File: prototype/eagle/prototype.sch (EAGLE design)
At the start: 45 parts, among them J4 USBSMD, T1 3904, U1 ATMEGA328, U2 ATA6631, U3 ATA6631, U5 FT232RL, X1 16MHz

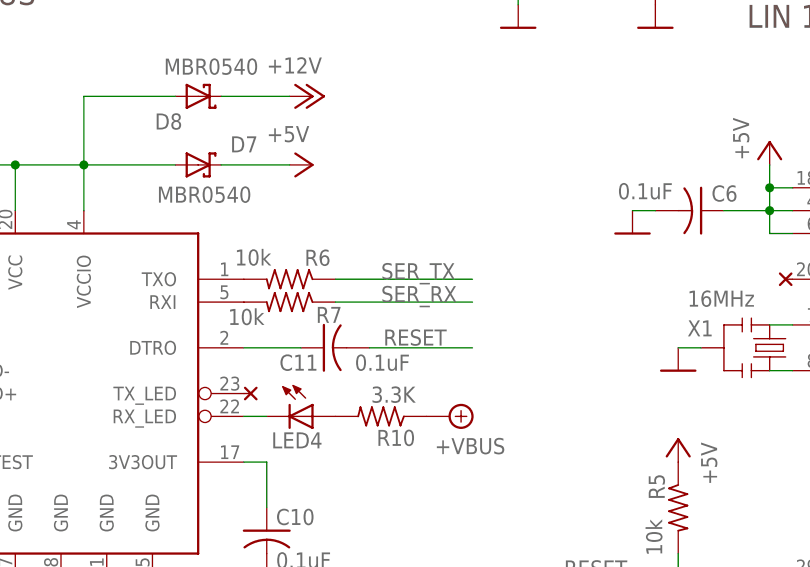
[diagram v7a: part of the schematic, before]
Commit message: Cleaned up the proxying code.
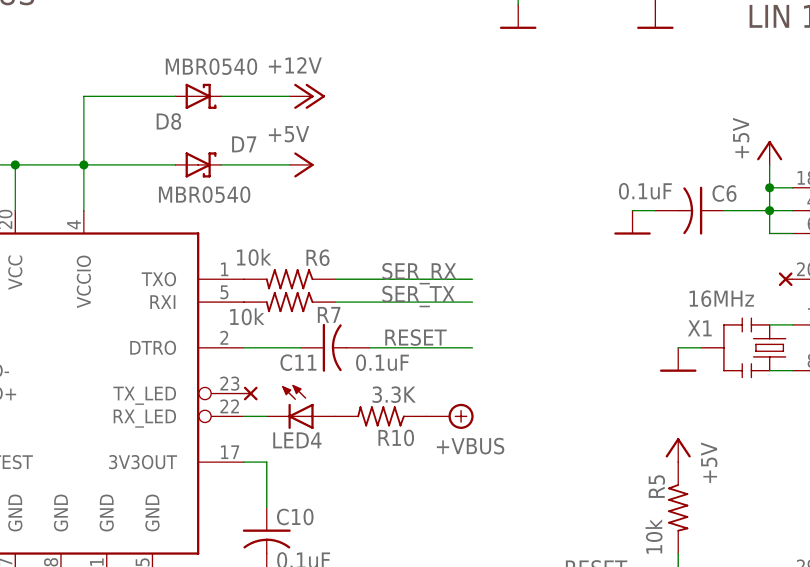
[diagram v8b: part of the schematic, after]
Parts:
- U1: device prototype:ATMEGA328 -> beeper:ATMEGA328
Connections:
- net SER_RX: now also R6.1; no longer R7.1
- net SER_TX: now also R7.1; no longer R6.1
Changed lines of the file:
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@@
 <layer number="51" name="tDocu" color="6" fill="1" visible="no" active="no"/>
 <layer number="52" name="bDocu" color="7" fill="1" visible="no" active="no"/>
-<layer number="53" name="tGND_GNDA" color="7" fill="9" visible="no" active="no"/>
-<layer number="54" name="bGND_GNDA" color="1" fill="9" visible="no" active="no"/>
+<layer number="53" name="tGND_GNDA" color="7" fill="1" visible="no" active="no"/>
+<layer number="54" name="bGND_GNDA" color="7" fill="1" visible="no" active="no"/>
 <layer number="56" name="wert" color="7" fill="1" visible="no" active="no"/>
 <layer number="91" name="Nets" color="2" fill="1" visible="yes" active="yes"/>
@@
 <layer number="97" name="Info" color="12" fill="1" visible="yes" active="yes"/>
 <layer number="98" name="Guide" color="6" fill="1" visible="yes" active="yes"/>
-<layer number="100" name="Muster" color="7" fill="1" visible="no" active="no"/>
-<layer number="101" name="Patch_Top" color="12" fill="4" visible="yes" active="yes"/>
+<layer number="100" name="Muster" color="7" fill="1" visible="yes" active="yes"/>
+<layer number="101" name="Patch_Top" color="7" fill="1" visible="yes" active="yes"/>
 <layer number="102" name="Vscore" color="7" fill="1" visible="yes" active="yes"/>
 <layer number="103" name="tMap" color="7" fill="1" visible="yes" active="yes"/>
@@
 <layer number="106" name="bPlate" color="7" fill="1" visible="yes" active="yes"/>
 <layer number="107" name="Crop" color="7" fill="1" visible="yes" active="yes"/>
-<layer number="116" name="Patch_BOT" color="9" fill="4" visible="yes" active="yes"/>
+<layer number="116" name="Patch_BOT" color="7" fill="1" visible="yes" active="yes"/>
 <layer number="121" name="_tsilk" color="7" fill="1" visible="yes" active="yes"/>
 <layer number="122" name="_bsilk" color="7" fill="1" visible="yes" active="yes"/>
-<layer number="125" name="_tNames" color="7" fill="1" visible="no" active="yes"/>
+<layer number="125" name="_tNames" color="7" fill="1" visible="yes" active="yes"/>
 <layer number="144" name="Drill_legend" color="7" fill="1" visible="yes" active="yes"/>
 <layer number="151" name="HeatSink" color="7" fill="1" visible="yes" active="yes"/>
-<layer number="200" name="200bmp" color="1" fill="10" visible="no" active="no"/>
-<layer number="201" name="201bmp" color="2" fill="1" visible="no" active="no"/>
-<layer number="202" name="202bmp" color="3" fill="1" visible="no" active="no"/>
-<layer number="203" name="203bmp" color="4" fill="10" visible="yes" active="yes"/>
-<layer number="204" name="204bmp" color="5" fill="10" visible="yes" active="yes"/>
-<layer number="205" name="205bmp" color="6" fill="10" visible="yes" active="yes"/>
-<layer number="206" name="206bmp" color="7" fill="10" visible="yes" active="yes"/>
-<layer number="207" name="207bmp" color="8" fill="10" visible="yes" active="yes"/>
-<layer number="208" name="208bmp" color="9" fill="10" visible="yes" active="yes"/>
+<layer number="200" name="200bmp" color="7" fill="1" visible="yes" active="yes"/>
+<layer number="201" name="201bmp" color="7" fill="1" visible="yes" active="yes"/>
+<layer number="202" name="202bmp" color="7" fill="1" visible="yes" active="yes"/>
+<layer number="203" name="203bmp" color="7" fill="1" visible="yes" active="yes"/>
+<layer number="204" name="204bmp" color="7" fill="1" visible="yes" active="yes"/>
+<layer number="205" name="205bmp" color="7" fill="1" visible="yes" active="yes"/>
+<layer number="206" name="206bmp" color="7" fill="1" visible="yes" active="yes"/>
+<layer number="207" name="207bmp" color="7" fill="1" visible="yes" active="yes"/>
+<layer number="208" name="208bmp" color="7" fill="1" visible="yes" active="yes"/>
 <layer number="209" name="209bmp" color="7" fill="1" visible="yes" active="yes"/>
 <layer number="210" name="210bmp" color="7" fill="1" visible="yes" active="yes"/>
@@
 <layer number="215" name="215bmp" color="7" fill="1" visible="yes" active="yes"/>
 <layer number="216" name="216bmp" color="7" fill="1" visible="yes" active="yes"/>
-<layer number="217" name="217bmp" color="18" fill="1" visible="no" active="no"/>
-<layer number="218" name="218bmp" color="19" fill="1" visible="no" active="no"/>
-<layer number="219" name="219bmp" color="20" fill="1" visible="no" active="no"/>
-<layer number="220" name="220bmp" color="21" fill="1" visible="no" active="no"/>
-<layer number="221" name="221bmp" color="22" fill="1" visible="no" active="no"/>
-<layer number="222" name="222bmp" color="23" fill="1" visible="no" active="no"/>
-<layer number="223" name="223bmp" color="24" fill="1" visible="no" active="no"/>
-<layer number="224" name="224bmp" color="25" fill="1" visible="no" active="no"/>
-<layer number="250" name="Descript" color="3" fill="1" visible="no" active="no"/>
-<layer number="251" name="SMDround" color="12" fill="11" visible="no" active="no"/>
+<layer number="217" name="217bmp" color="7" fill="1" visible="yes" active="yes"/>
+<layer number="218" name="218bmp" color="7" fill="1" visible="yes" active="yes"/>
+<layer number="219" name="219bmp" color="7" fill="1" visible="yes" active="yes"/>
+<layer number="220" name="220bmp" color="7" fill="1" visible="yes" active="yes"/>
+<layer number="221" name="221bmp" color="7" fill="1" visible="yes" active="yes"/>
+<layer number="222" name="222bmp" color="7" fill="1" visible="yes" active="yes"/>
+<layer number="223" name="223bmp" color="7" fill="1" visible="yes" active="yes"/>
+<layer number="224" name="224bmp" color="7" fill="1" visible="yes" active="yes"/>
+<layer number="250" name="Descript" color="7" fill="1" visible="yes" active="yes"/>
+<layer number="251" name="SMDround" color="7" fill="1" visible="yes" active="yes"/>
 <layer number="254" name="cooling" color="7" fill="1" visible="yes" active="yes"/>
 </layers>
@@
 <part name="GND29" library="prototype" deviceset="GND" device=""/>
 <part name="U$2" library="prototype" deviceset="NC" device=""/>
-<part name="U1" library="prototype" deviceset="ATMEGA328" device="" value="ATMEGA328"/>
+<part name="U1" library="beeper" deviceset="ATMEGA328" device="" value="ATMEGA328"/>
 <part name="X1" library="prototype" deviceset="RESONATOR" device="SMD" value="16MHz"/>
 <part name="GND4" library="prototype" deviceset="GND" device=""/>
@@
 <net name="SER_TX" class="0">
 <segment>
+<pinref part="U1" gate="G$1" pin="PD1(TXD)"/>
+<wire x1="223.52" y1="116.84" x2="243.84" y2="116.84" width="0.1524" layer="91"/>
+<label x="226.06" y="116.84" size="1.778" layer="95"/>
+</segment>
+<segment>
+<pinref part="R7" gate="G$1" pin="1"/>
+<wire x1="124.46" y1="129.54" x2="139.7" y2="129.54" width="0.1524" layer="91"/>
+<label x="129.54" y="129.54" size="1.778" layer="95"/>
+</segment>
+</net>
+<net name="SER_RX" class="0">
+<segment>
+<pinref part="U1" gate="G$1" pin="PD0(RXD)"/>
+<wire x1="223.52" y1="119.38" x2="243.84" y2="119.38" width="0.1524" layer="91"/>
+<label x="226.06" y="119.38" size="1.778" layer="95"/>
+</segment>
+<segment>
 <pinref part="R6" gate="G$1" pin="1"/>
 <wire x1="139.7" y1="132.08" x2="124.46" y2="132.08" width="0.1524" layer="91"/>
 <label x="129.54" y="132.08" size="1.778" layer="95"/>
 </segment>
-<segment>
-<pinref part="U1" gate="G$1" pin="PD1(TXD)"/>
-<wire x1="223.52" y1="116.84" x2="243.84" y2="116.84" width="0.1524" layer="91"/>
-<label x="226.06" y="116.84" size="1.778" layer="95"/>
-</segment>
-</net>
-<net name="SER_RX" class="0">
-<segment>
-<pinref part="R7" gate="G$1" pin="1"/>
-<wire x1="139.7" y1="129.54" x2="124.46" y2="129.54" width="0.1524" layer="91"/>
-<label x="129.54" y="129.54" size="1.778" layer="95"/>
-</segment>
-<segment>
-<pinref part="U1" gate="G$1" pin="PD0(RXD)"/>
-<wire x1="223.52" y1="119.38" x2="243.84" y2="119.38" width="0.1524" layer="91"/>
-<label x="226.06" y="119.38" size="1.778" layer="95"/>
-</segment>
-</net>
+</net>
